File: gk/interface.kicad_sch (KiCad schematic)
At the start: 64 parts, among them J11 Conn_01x02, J7 Conn_01x02, SW3 RotaryEncoder_Switch, U9 LSM6DSL

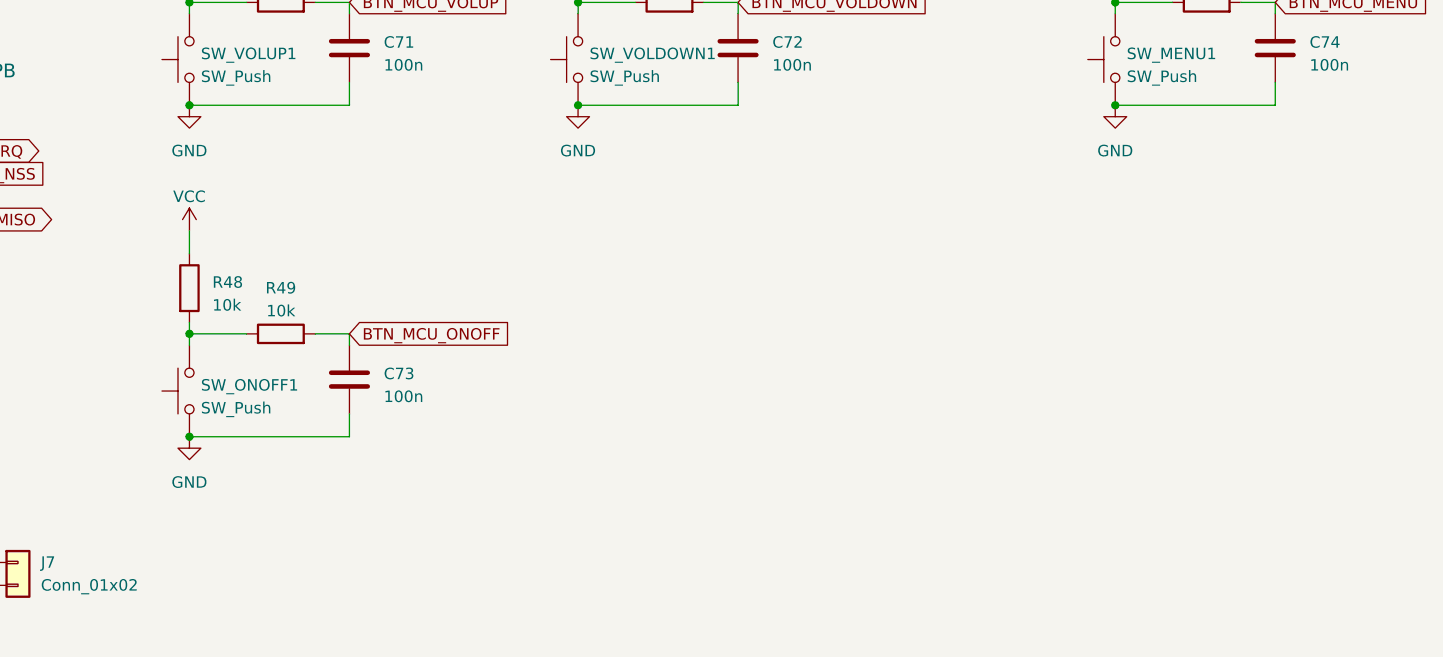
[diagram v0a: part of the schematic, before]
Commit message: update power button routing
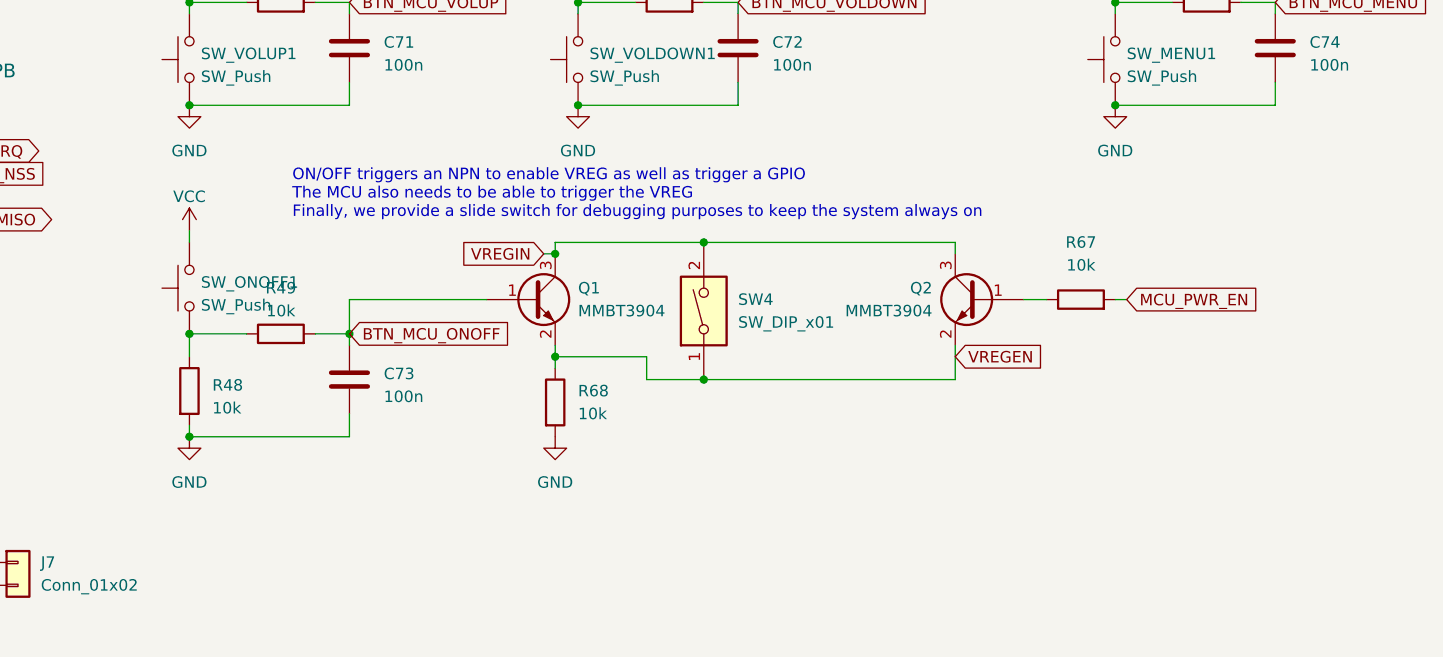
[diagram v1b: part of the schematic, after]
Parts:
- added Q1, Q2: MMBT3904, Package_TO_SOT_SMD:SOT-23, symbol Transistor_BJT:MMBT3904
- added R67, R68: 10k, Resistor_SMD:R_0603_1608Metric, symbol Device:R
- added SW4: SW_DIP_x01, Button_Switch_THT:SW_DIP_SPSTx01_Slide_9.78x4.72mm_W7.62mm_P2.54mm, symbol Switch:SW_DIP_x01
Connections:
- net BTN_MCU_ONOFF: now also Q1.1 (B)
- net GND: now also R48.2, R68.2; no longer SW_ONOFF1.1
- net VCC: now also SW_ONOFF1.2; no longer R48.1
- new net: R48.1, R49.1, SW_ONOFF1.1
- new net: Q2.1 (B), R67.1
- new net MCU_PWR_EN: R67.2
- new net VREGEN: Q1.2 (E), Q2.2 (E), R68.1, SW4.1
- new net VREGIN: Q1.3 (C), Q2.3 (C), SW4.2
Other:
- note added: "ON/OFF triggers an NPN to enable VREG as well as trigger a GPIO The MCU also needs to be able to trigger the VREG Finally, we provide a slide switch for debugging purposes to keep the system always on"
- moved on the sheet: R48, SW_ONOFF1
